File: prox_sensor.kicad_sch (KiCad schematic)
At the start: 14 parts, among them J1 +, J2 -, J3 A, J9 K, U1 BD4840G-TR, U6 NCP718xSN330

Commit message: Rev 4: separating sensors
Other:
- title: COB Driver Board -> Li-ion
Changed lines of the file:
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@@
 	(paper "A4")
 	(title_block
-		(title "COB Driver Board")
+		(title "Li-ion")
+		(date "2025-03-21")
+		(rev "1")
 	)
 	(text "No Logo Assigned"
@@
 			"AAAAAAAAAAAAAAAAAAAAAAAAAAAAAAAAAAAAAAAAAAAAAAAAAAAAAAAAAAAAAAAAAAAAAAAAAAAA"
 			"AAAAAAAAAAAAAAAAAAAAAAAAAAAAAAAAAAAAAAAAAAAAAAAAAAAAAAAAAAAAAAAAAAAAAAAAAAAA"
+			"AAAAAAAAAAAAAAAAAAAAAAAAAAAAAAAAAAAAAAAAAAAAAAAAAAAAAAAAAAAAAAAAAAAAAAAAAAAA"
+			"AAAAAAAAAAAAAAAAAAAAAAAAAAAAAAAAAAAAAAAAAAAAAAAAAAAAAAAAAAAAAAAAAAAAAAAAAAAA"
+			"AAAAAAAAAAAAAAAAAAAAAAAAAAAAAAAAAAAAAAAAAAAAAAAAAAAAAAAAAAAAAAAAAAAAAAAAAAAA"
+			"AAAAAAAAAAAAAAAAAAAAAAAAAAAAAAAAAAAAAAAAAAAAAAAAAAAAAAAAAAAAAAAAAAAAAAAAAAAA"
+			"AAAAAAAAAAAAAAAAAAAAAAAAAAAAAAAAAAAAAAAAAAAAAAAAAAAAAAAAAAAAAAAAAAAAAAAAAAAA"
+			"AAAAAAAAAAAAAAAAAAAAAAAAAAAAAAAAAAAAAAAAAAAAAAAAAAAAAAAAAAAAAAAAAAAAAAAAAAAA"
+			"AAAAAAAAAAAAAAAAAAAAAAAAAAAAAAAAAAAAAAAAAAAAAAAAAAAAAAAAAAAAAAAAAAAAAAAAAAAA"
+			"AAAAAAAAAAAAAAAAAAAAAAAAAAAAAAAAAAAAAAAAAAAAAAAAAAAAAAAAAAAAAAAAAAAAAAAAAAAA"
+			"AAAAAAAAAAAAAAAAAAAAAAAAAAAAAAAAAAAAAAAAAAAAAAAAAAAAAAAAAAAAAAAAAAAAAAAAAAAA"
+			"AAAAAAAAAAAAAAAAAAAAAAAAAAAAAAAAAAAAAAAAAAAAAAAAAAAAAAAAAAAAAAAAAAAAAAAAAAAA"
+			"AAAAAAAAAAAAAAAAAAAAAAAAAAAAAAAAAAAAAAAAAAAAAAAAAAAAAAAAAAAAAAAAAAAAAAAAAAAA"
+			"AAAAAAAAAAAAAAAAAAAAAAAAAAAAAAAAAAAAAAAAAAAAAAAAAAAAAAAAAAAAAAAAAAAAAAAAAAAA"
+			"AAAAAAAAAAAAAAAAAAAAAAAAAAAAAAAAAAAAAAAAAAAAAAAAAAAAAAAAAAAAAAAAAAAAAAAAAAAA"
+			"AAAAAAAAAAAAAAAAAAAAAAAAAAAAAAAAAAAAAAAAAAAAAAAAAAAAAAAAAAAAAAAAAAAAAAAAAAAA"
+			"AAAAAAAAAAAAAAAAAAAAAAAAAAAAAAAAAAAAAAAAAAAAAAAAAAAAAAAAAAAAAAAAAAAAAAAAAAAA"
+			"AAAAAAAAAAAAAAAAAAAAAAAAAAAAAAAAAAAAAAAAAAAAAAAAAAAAAAAAAAAAAAAAAAAAAAAAAAAA"
+			"AAAAAAAAAAAAAAAAAAAAAAAAAAAAAAAAAAAAAAAAAAAAAAAAAAAAAAAAAAAAAAAAAAAAAAAAAAAA"
+			"AAAAAAAAAAAAAAAAAAAAAAAAAAAAAAAAAAAAAAAAAAAAAAAAAAAAAAAAAAAAAAAAAAAAAAAAAAAA"

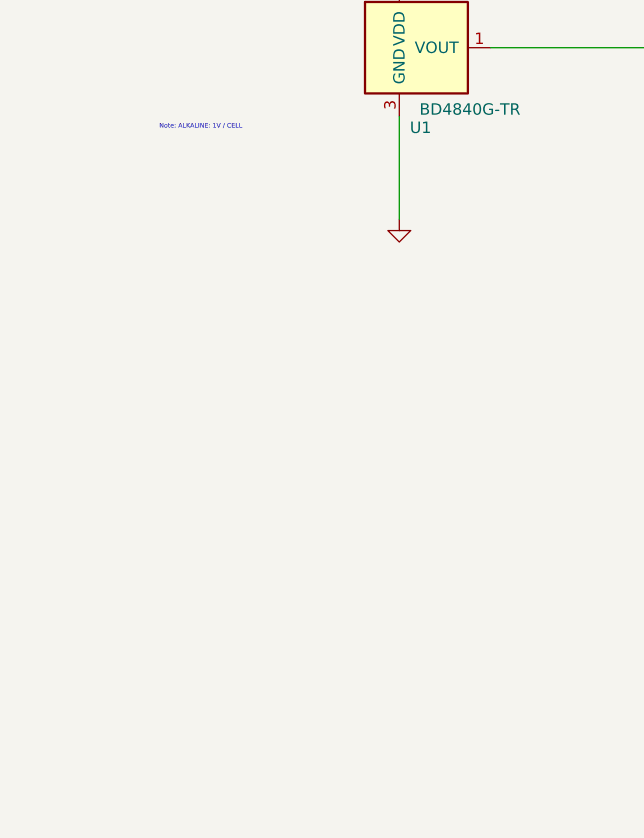
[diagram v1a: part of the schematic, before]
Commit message: Separate sensors, refactoring
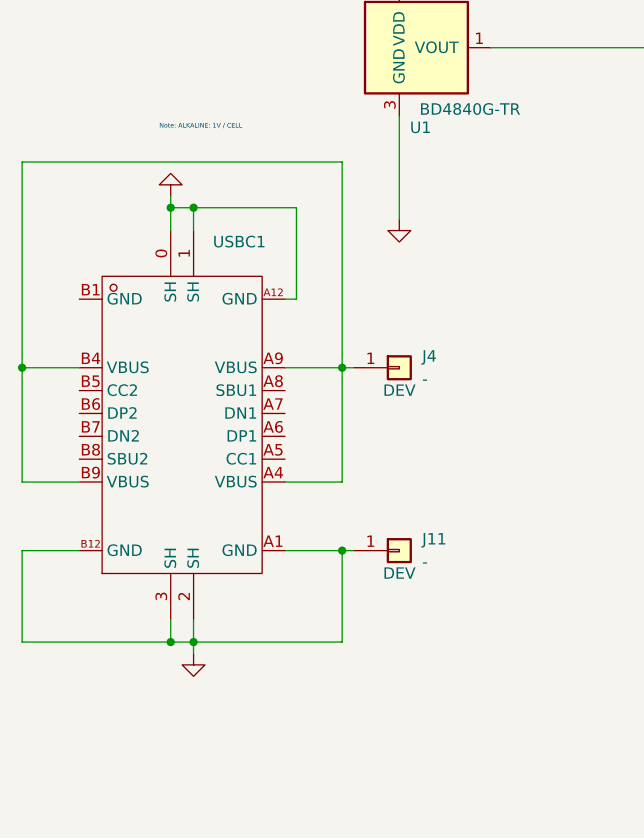
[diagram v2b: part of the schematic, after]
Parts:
- added J11, J4: -, TestPoint:TestPoint_Pad_D2.0mm, symbol Connector_Generic:Conn_01x01
- added USBC1: ~, 1-COB-MOD:USB-C_SMD-TYPE-C-31-M-12, symbol 1-cob-drv:TYPE-C-31-M-12
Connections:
- net GND: now also J11.1 (Pin_1), USBC1.0 (SH), USBC1.1 (SH), USBC1.2 (SH), USBC1.3 (SH), USBC1.A1 (GND), USBC1.A12 (GND), USBC1.B12 (GND)
- new net: J4.1 (Pin_1), USBC1.A4 (VBUS), USBC1.A9 (VBUS), USBC1.B4 (VBUS), USBC1.B9 (VBUS)

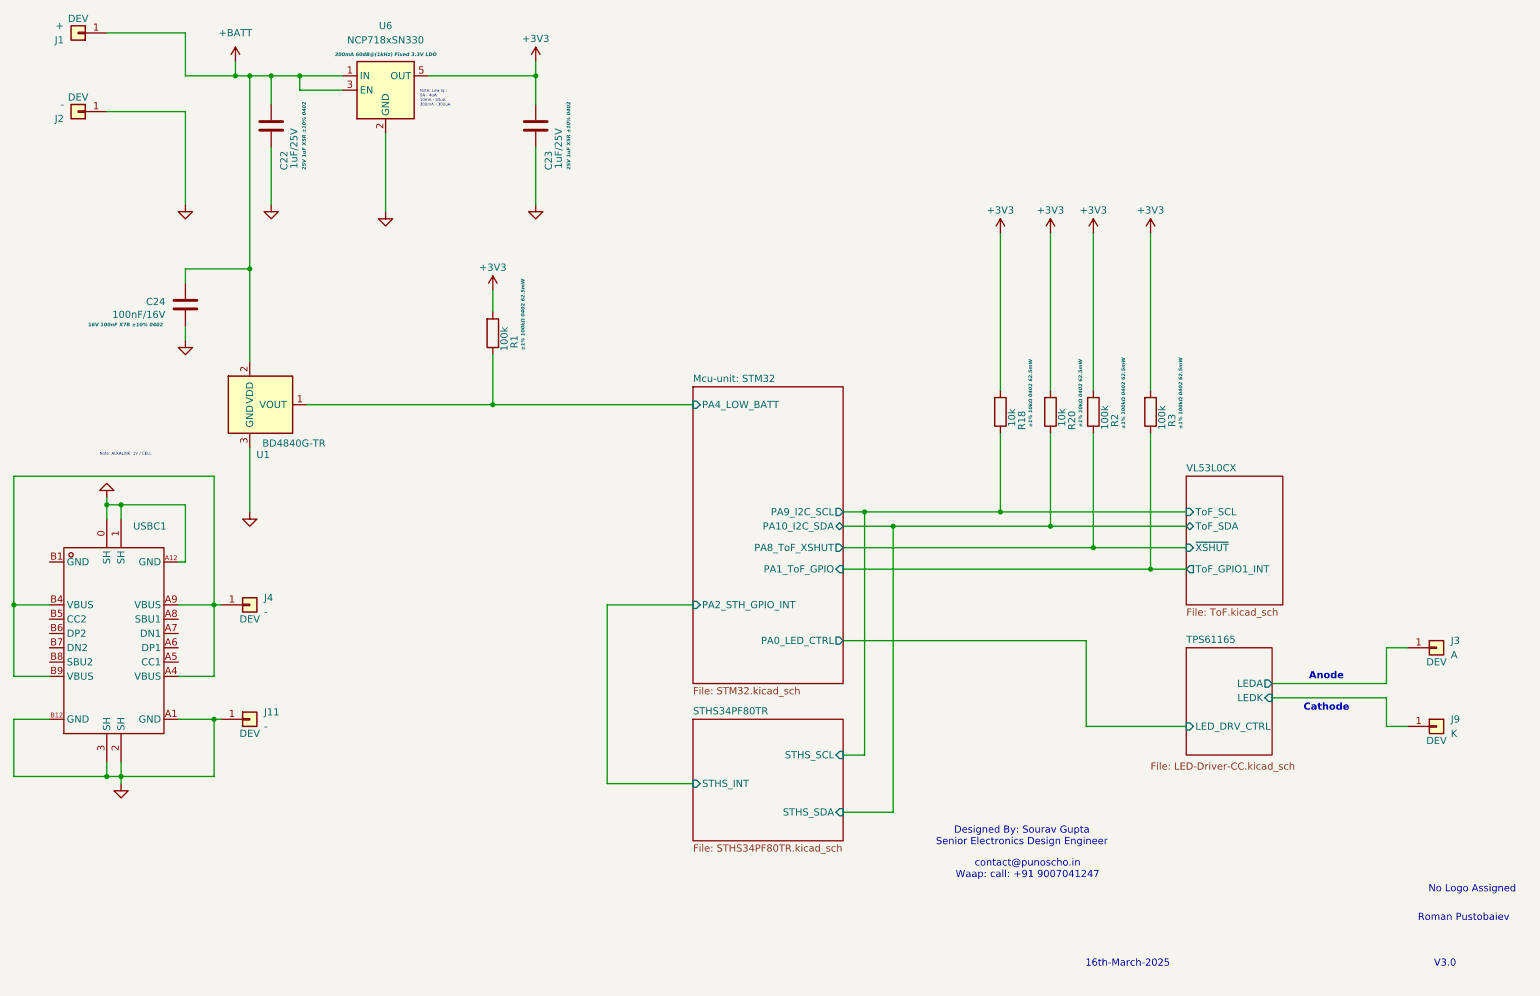
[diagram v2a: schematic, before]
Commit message: Adding light sensor
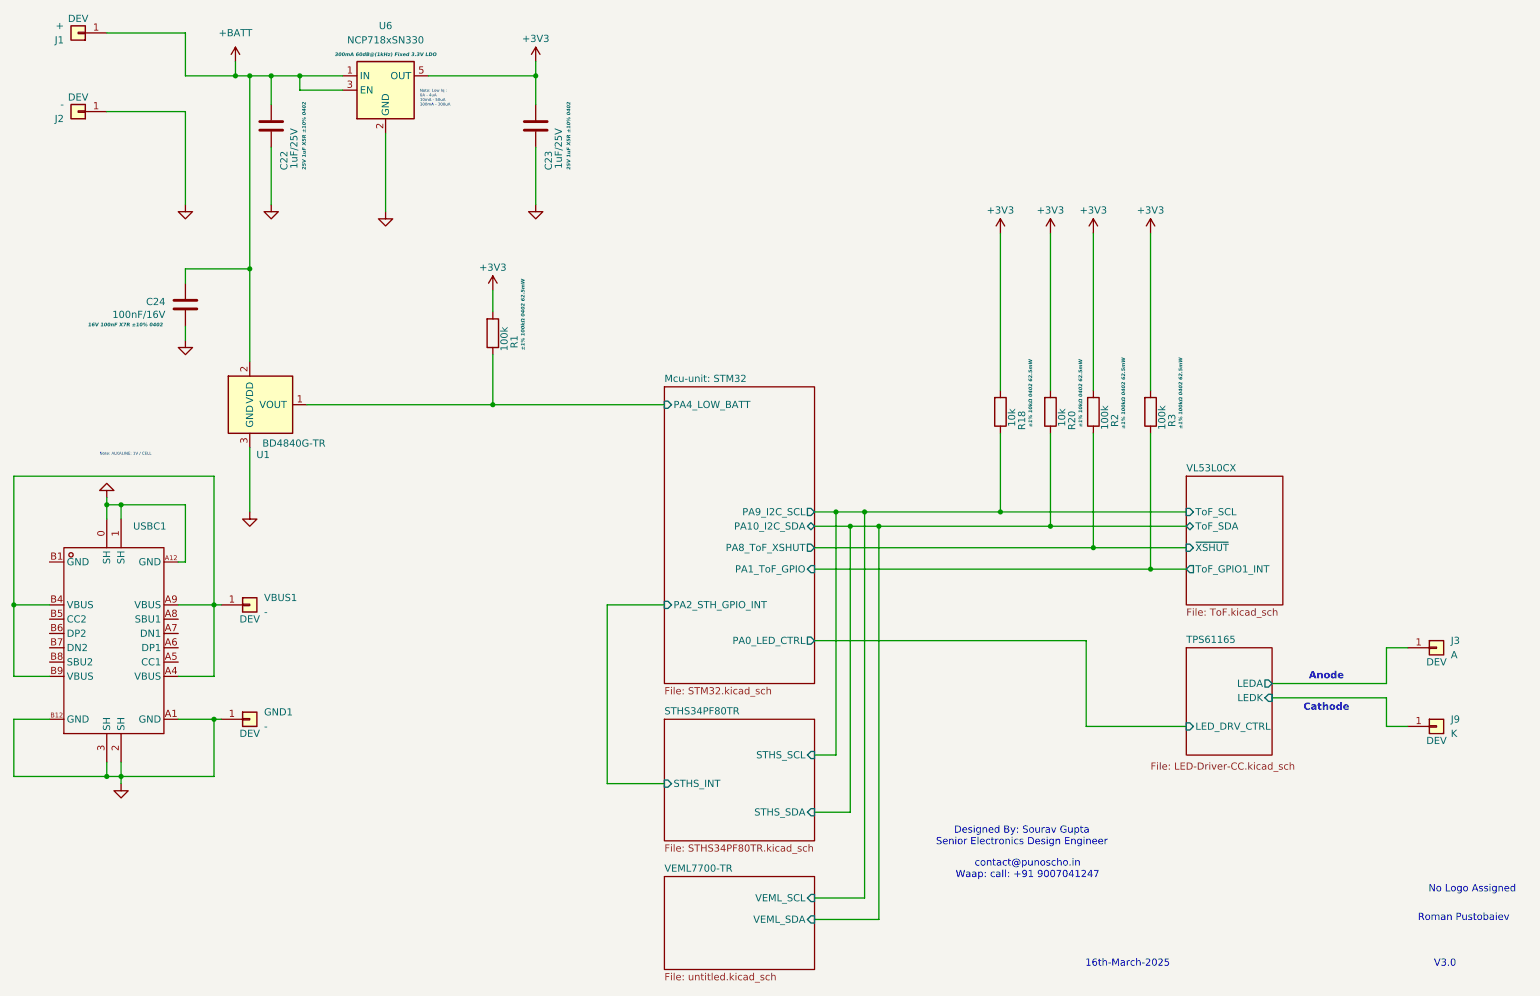
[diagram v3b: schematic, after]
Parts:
- renumbered J11 to GND1, J4 to VBUS1
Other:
- added sheet VEML7700-TR (untitled.kicad_sch)
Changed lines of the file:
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@@
 	)
 	(junction
-		(at 167.64 113.03)
-		(diameter 0)
-		(color 0 0 0 0)
-	)
-	(junction
 		(at 58.42 35.56)
 		(diameter 0)
@@
 	)
 	(junction
-		(at 172.72 115.57)
+		(at 33.02 111.76)
 		(diameter 0)
 		(color 0 0 0 0)
 	)
 	(junction
-		(at 33.02 111.76)
+		(at 55.88 35.56)
 		(diameter 0)
 		(color 0 0 0 0)
 	)
 	(junction
-		(at 55.88 35.56)
+		(at 208.28 119.38)
 		(diameter 0)
 		(color 0 0 0 0)
 	)
 	(junction
-		(at 208.28 119.38)
+		(at 170.18 115.57)
 		(diameter 0)
 		(color 0 0 0 0)
@@
 	)
 	(junction
+		(at 167.64 113.03)
+		(diameter 0)
+		(color 0 0 0 0)
+	)
+	(junction
 		(at 191.77 113.03)
 		(diameter 0)
@@
 	)
 	(junction
+		(at 165.1 115.57)
+		(diameter 0)
+		(color 0 0 0 0)
+	)
+	(junction
+		(at 162.56 113.03)
+		(diameter 0)
+		(color 0 0 0 0)
+	)
+	(junction
 		(at 200.66 115.57)
 		(diameter 0)
@@
 	(wire
 		(pts
-			(xy 172.72 166.37) (xy 172.72 115.57)
+			(xy 165.1 166.37) (xy 165.1 115.57)
 		)
 		(stroke
@@
 	(wire
 		(pts
-			(xy 172.72 115.57) (xy 200.66 115.57)
-		)
-		(stroke
-			(width 0)
-			(type default)
-		)
-	)
-	(wire
-		(pts
 			(xy 218.44 99.06) (xy 218.44 123.19)
 		)
@@
 	(wire
 		(pts
-			(xy 163.83 119.38) (xy 208.28 119.38)
+			(xy 158.75 119.38) (xy 208.28 119.38)
 		)
 		(stroke
@@
 	(wire
 		(pts
-			(xy 163.83 135.89) (xy 207.01 135.89)
+			(xy 158.75 135.89) (xy 207.01 135.89)
 		)
 		(stroke
@@
 	(wire
 		(pts
-			(xy 163.83 113.03) (xy 167.64 113.03)
+			(xy 158.75 113.03) (xy 162.56 113.03)
 		)
 		(stroke
@@
 	(wire
 		(pts
-			(xy 137.16 129.54) (xy 121.92 129.54)
+			(xy 132.08 129.54) (xy 121.92 129.54)
+		)
+		(stroke
+			(width 0)
+			(type default)
+		)
+	)
+	(wire
+		(pts
+			(xy 165.1 115.57) (xy 170.18 115.57)
+		)
+		(stroke
+			(width 0)
+			(type default)
+		)
+	)
+	(wire
+		(pts
+			(xy 158.75 181.61) (xy 167.64 181.61)
 		)
 		(stroke
@@
 	(wire
 		(pts
-			(xy 167.64 113.03) (xy 191.77 113.03)
+			(xy 167.64 181.61) (xy 167.64 113.03)
 		)
 		(stroke
@@
 	(wire
 		(pts
-			(xy 163.83 156.21) (xy 167.64 156.21)
+			(xy 158.75 156.21) (xy 162.56 156.21)
 		)
 		(stroke
@@
 	(wire
 		(pts
-			(xy 163.83 166.37) (xy 172.72 166.37)
+			(xy 158.75 166.37) (xy 165.1 166.37)
 		)
 		(stroke
@@
 	(wire
 		(pts
-			(xy 101.6 93.98) (xy 137.16 93.98)
+			(xy 101.6 93.98) (xy 132.08 93.98)
 		)
 		(stroke
@@
 	(wire
 		(pts
+			(xy 170.18 185.42) (xy 170.18 115.57)
+		)
+		(stroke
+			(width 0)
+			(type default)
+		)
+	)
+	(wire
+		(pts
 			(xy 33.02 160.02) (xy 35.56 160.02)
 		)
@@
 	(wire
 		(pts
+			(xy 162.56 113.03) (xy 167.64 113.03)
+		)
+		(stroke
+			(width 0)
+			(type default)
+		)
+	)
+	(wire
+		(pts
 			(xy 22.86 149.86) (xy 16.51 149.86)
 		)
@@
 	(wire
 		(pts
-			(xy 121.92 161.29) (xy 137.16 161.29)
+			(xy 167.64 113.03) (xy 191.77 113.03)
+		)
+		(stroke
+			(width 0)
+			(type default)
+		)
+	)
+	(wire
+		(pts
+			(xy 121.92 161.29) (xy 132.08 161.29)
 		)
 		(stroke
@@
 	(wire
 		(pts
-			(xy 163.83 115.57) (xy 172.72 115.57)
+			(xy 158.75 115.57) (xy 165.1 115.57)
 		)
 		(stroke
@@
 	(wire
 		(pts
-			(xy 218.44 123.19) (xy 163.83 123.19)
+			(xy 218.44 123.19) (xy 158.75 123.19)
 		)
 		(stroke
@@
 	(wire
 		(pts
+			(xy 170.18 115.57) (xy 200.66 115.57)
+		)
+		(stroke
+			(width 0)
+			(type default)
+		)
+	)
+	(wire
+		(pts
 			(xy 16.51 106.68) (xy 52.07 106.68)
 		)
@@
 	(wire
 		(pts
-			(xy 167.64 156.21) (xy 167.64 113.03)
+			(xy 162.56 156.21) (xy 162.56 113.03)
 		)
 		(stroke
@@
 		)
 	)
+	(wire
+		(pts
+			(xy 158.75 185.42) (xy 170.18 185.42)
+		)
+		(stroke
+			(width 0)
+			(type default)
+		)
+	)
 	(image
 		(at 36.83 93.98)
@@
 			"AG4AAABlAAAAcgAAAGEAAAB0AAAAbwAAAHIAAAAQ/QMAAAAAAHAAAAAAAAAAQryqKypWAABuAAAA"
 			"bgAAAGUAAABjAAAAdAAAAG8AAAByAAAAIAAAAEoAAABBAAAARQAAACAAAAAgAAAAcwAAAGkAAABk"
-			"AAAAZQAAACAAAA=="
+			"AAAAZQAAACAAAAAAAAAAAAAAAAAAAAAAAAAAAAAAAAAAAAAAAAAAAAAAAAAAAAAAAAAAAAAAAAAA"
+			"AAAAAAAAAAAAAAAAAAAAAAAAAAAAAAAAAAAAAAAAAAAAAAAAAAAAAAAAAAAAAAAAAAAAAAAAAAAA"
+			"AAAAAAAAAAAAAAAAAAAAAAAAAAAAAAAAAAAAAAAAAAAAAAAAAAAAAAAAAAAAAAAAAAAAAAAAAAAA"
+			"AAAAAAAAAAAAAAAAAAAAAAAAAAAAAAAAAAAAAAAAAAAAAAAAAAAAAAAAAAAAAAAAAAAAAAAAAAAA"
+			"AAAAAAAAAAAAAAAAAAAAAAAAAAAAAAAAAAAAAAAAAAAAAAAAAAAAAAAAAAAAAAAAAAAAAAAAAAAA"
+			"AAAAAAAAAAAAAAAAAAAAAAAAAAAAAAAAAAAAAAAAAAAAAAAAAAAAAAAAAAAAAAAAAAAAAAAAAAAA"
+			"AAAAAAAAAAAAAAAAAAAAAAAAAAAAAAAAAAAAAAAAAAAAAAAAAAAAAAAAAAAAAAAAAAAAAAAAAAAA"
+			"AAAAAAAAAAAAAAAAAAAAAAAAAAAAAAAAAAAAAAAAAAAAAAAAAAAAAAAAAAAAAAAAAAAAAAAAAAAA"
+			"AAAAAAAAAAAAAAAAAAAAAAAAAAAAAAAAAAAAAAAAAAAAAAAAAAAAAAAAAAAAAAAAAAAAAAAAAAAA"
+			"AAAAAAAAAAAAAAAAAAAAAAAAAAAAAAAAAAAAAAAAAAAAAAAAAAAAAAAAAAAAAAAAAAAAAAAAAAAA"
+			"AAAAAAAAAAAAAAAAAAAAAAAAAAAAAAAAAAAAAAAAAAAAAAAAAAAAAAAAAAAAAAAAAAAAAAAAAAAA"
+			"AAAAAAAAAAAAAAAAAAAAAAAAAAAAAAAAAAAAAAAAAAAAAAAAAAAAAAAAAAAAAAAAAAAAAAAAAAAA"
+			"AAAAAAAAAAAAAAAAAAAAAAAAAAAAAAAAAAAAAAAAAAAAAAAAAAAAAAAAAAAAAAAAAAAAAAAAAAAA"
+			"AAAAAAAAAAAAAAAAAAAAAAAAAAAAAAAAAAAAAAAAAAAAAAAAAAAAAAAAAAAAAAAAAAAAAAAAAAAA"
+			"AAAAAAAAAAAAAAAAAAAAAAAAAAAAAAAAAAAAAAAAAAAAAAAAAAAAAAAAAAAAAAAAAAAAAAAAAAAA"
+			"AAAAAAAAAAAAAAAAAAAAAAAAAAAAAAAAAAAAAAAAAAAAAAAAAAAAAAAAAAAAAAAAAAAAAAAAAAAA"
+			"AAAAAAAAAAAAAAAAAAAAAAAAAAAAAAAAAAAAAAAAAAAAAAAAAAAAAAAAAAAAAAAAAAAAAAAAAAAA"
+			"AAAAAAAAAAAAAAAAAAAAAAAAAAAAAAAAAAAAAAAAAAAAAAAAAAAAAAAAAAAAAAAAAAAAAAAAAAAA"
+			"AAAAAAAAAAAAAA=="
 		)
 	)
@@
 		(on_board yes)
 		(dnp no)
-		(property "Reference" "J11"
+		(property "Reference" "GND1"
 			(at 60.96 148.5899 0)
 			(effects
@@
 			(project "prox_sensor"
 				(path "/72306bb1-8a24-469b-bdd7-d5938b058a41"
-					(reference "J11")
+					(reference "GND1")
 					(unit 1)
 				)
@@
 		(on_board yes)
 		(dnp no)
-		(property "Reference" "J4"
+		(property "Reference" "VBUS1"
 			(at 60.96 128.2699 0)
 			(effects
@@
 			(project "prox_sensor"
 				(path "/72306bb1-8a24-469b-bdd7-d5938b058a41"
-					(reference "J4")
+					(reference "VBUS1")
 					(unit 1)
 				)
@@
 	)
 	(sheet
-		(at 137.16 90.805)
+		(at 132.08 90.805)
 		(size 26.67 52.705)
 		(exclude_from_sim no)
@@
 		)
 		(property "Sheetname" "Mcu-unit: STM32"
-			(at 137.16 90.0934 0)
+			(at 132.08 90.0934 0)
 			(effects
 				(font
@@
 		)
 		(property "Sheetfile" "STM32.kicad_sch"
-			(at 137.16 144.0946 0)
+			(at 132.08 144.0946 0)
 			(effects
 				(font
@@
 		)
 		(pin "PA9_I2C_SCL" output
-			(at 163.83 113.03 0)
+			(at 158.75 113.03 0)
 			(effects
 				(font
@@
 		)
 		(pin "PA10_I2C_SDA" bidirectional
-			(at 163.83 115.57 0)
+			(at 158.75 115.57 0)
 			(effects
 				(font
@@
 		)
 		(pin "PA8_ToF_XSHUT" output
-			(at 163.83 119.38 0)
+			(at 158.75 119.38 0)
 			(effects
 				(font
@@
 		)
 		(pin "PA0_LED_CTRL" output
-			(at 163.83 135.89 0)
+			(at 158.75 135.89 0)
 			(effects
 				(font
@@
 		)
 		(pin "PA1_ToF_GPIO" input
-			(at 163.83 123.19 0)
+			(at 158.75 123.19 0)
 			(effects
 				(font
@@
 		)
 		(pin "PA4_LOW_BATT" input
-			(at 137.16 93.98 180)
+			(at 132.08 93.98 180)
 			(effects
 				(font
@@
 		)
 		(pin "PA2_STH_GPIO_INT" input
-			(at 137.16 129.54 180)
+			(at 132.08 129.54 180)
 			(effects
 				(font
@@
 	)
 	(sheet
-		(at 137.16 149.86)
+		(at 132.08 177.8)
+		(size 26.67 16.51)
+		(exclude_from_sim no)
+		(in_bom yes)
+		(on_board yes)
+		(dnp no)
+		(fields_autoplaced yes)
+		(stroke
+			(width 0.1524)
+			(type solid)
+		)
+		(fill
+			(color 0 0 0 0.0000)
+		)
+		(property "Sheetname" "VEML7700-TR"
+			(at 132.08 177.0884 0)
+			(effects
+				(font
+					(size 1.27 1.27)
+				)
+				(justify left bottom)
+			)
+		)
+		(property "Sheetfile" "untitled.kicad_sch"
+			(at 132.08 194.8946 0)
+			(effects
+				(font
+					(size 1.27 1.27)
+				)
+				(justify left top)
+			)
+		)
+		(pin "VEML_SCL" input
+			(at 158.75 181.61 0)
+			(effects
+				(font
+					(size 1.27 1.27)
+				)
+				(justify right)
+			)
+		)
+		(pin "VEML_SDA" input
+			(at 158.75 185.42 0)
+			(effects
+				(font
+					(size 1.27 1.27)
+				)
+				(justify right)
+			)
+		)
+		(instances
+			(project "prox_sensor"
+				(path "/72306bb1-8a24-469b-bdd7-d5938b058a41"
+					(page "6")
+				)
+			)
+		)
+	)
+	(sheet
+		(at 132.08 149.86)
 		(size 26.67 21.59)
 		(exclude_from_sim no)
@@
 		)
 		(property "Sheetname" "STHS34PF80TR"
-			(at 137.16 149.1484 0)
+			(at 132.08 149.1484 0)
 			(effects
 				(font
@@
 		)
 		(property "Sheetfile" "STHS34PF80TR.kicad_sch"
-			(at 137.16 172.0346 0)
+			(at 132.08 172.0346 0)
 			(effects
 				(font
@@
 		)
 		(pin "STHS_INT" input
-			(at 137.16 161.29 180)
+			(at 132.08 161.29 180)
 			(effects
 				(font
@@
 		)
 		(pin "STHS_SCL" input
-			(at 163.83 156.21 0)
+			(at 158.75 156.21 0)
 			(effects
 				(font
@@
 		)
 		(pin "STHS_SDA" input
-			(at 163.83 166.37 0)
+			(at 158.75 166.37 0)
 			(effects
 				(font

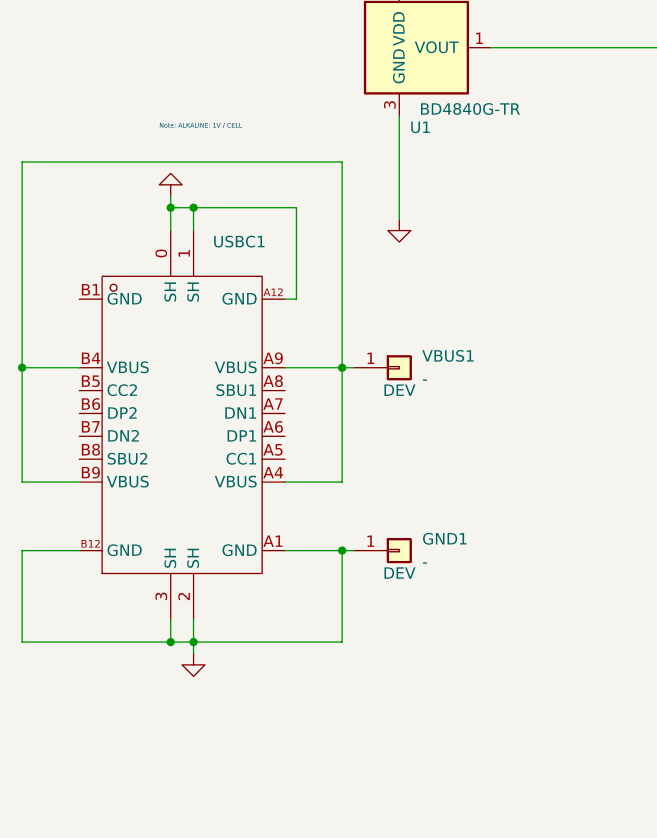
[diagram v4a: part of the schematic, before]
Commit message: Hole for VEML7700
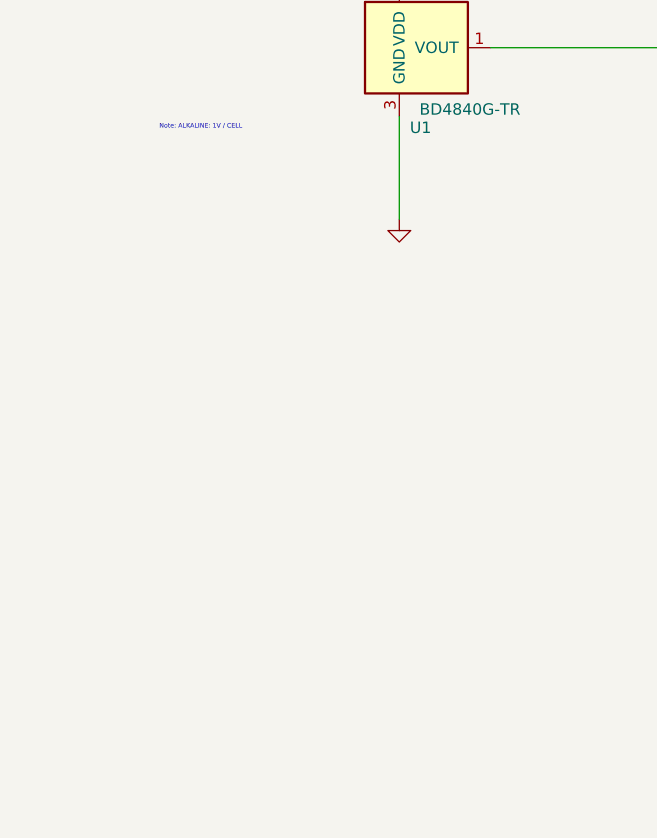
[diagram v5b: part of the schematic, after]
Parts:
- removed GND1, VBUS1: -, TestPoint:TestPoint_Pad_D2.0mm, symbol Connector_Generic:Conn_01x01
- removed USBC1: ~, 1-COB-MOD:USB-C_SMD-TYPE-C-31-M-12, symbol 1-cob-drv:TYPE-C-31-M-12

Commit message: Refactoring
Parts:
- added J10: K, Connector_PinHeader_1.27mm:PinHeader_1x01_P1.27mm_Vertical, symbol Connector_Generic:Conn_01x01
- added J4: A, Connector_PinHeader_1.27mm:PinHeader_1x01_P1.27mm_Vertical, symbol Connector_Generic:Conn_01x01
- J3, J9: footprint TestPoint:TestPoint_Pad_D2.0mm -> Connector_PinHeader_1.27mm:PinHeader_1x01_P1.27mm_Vertical
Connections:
- net TPS61165/LEDA: now also J4.1 (Pin_1)
- net TPS61165/LEDK: now also J10.1 (Pin_1)
